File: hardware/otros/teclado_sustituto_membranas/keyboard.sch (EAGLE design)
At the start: 98 parts, among them IC1 74HC32, IC2 74LS244DW

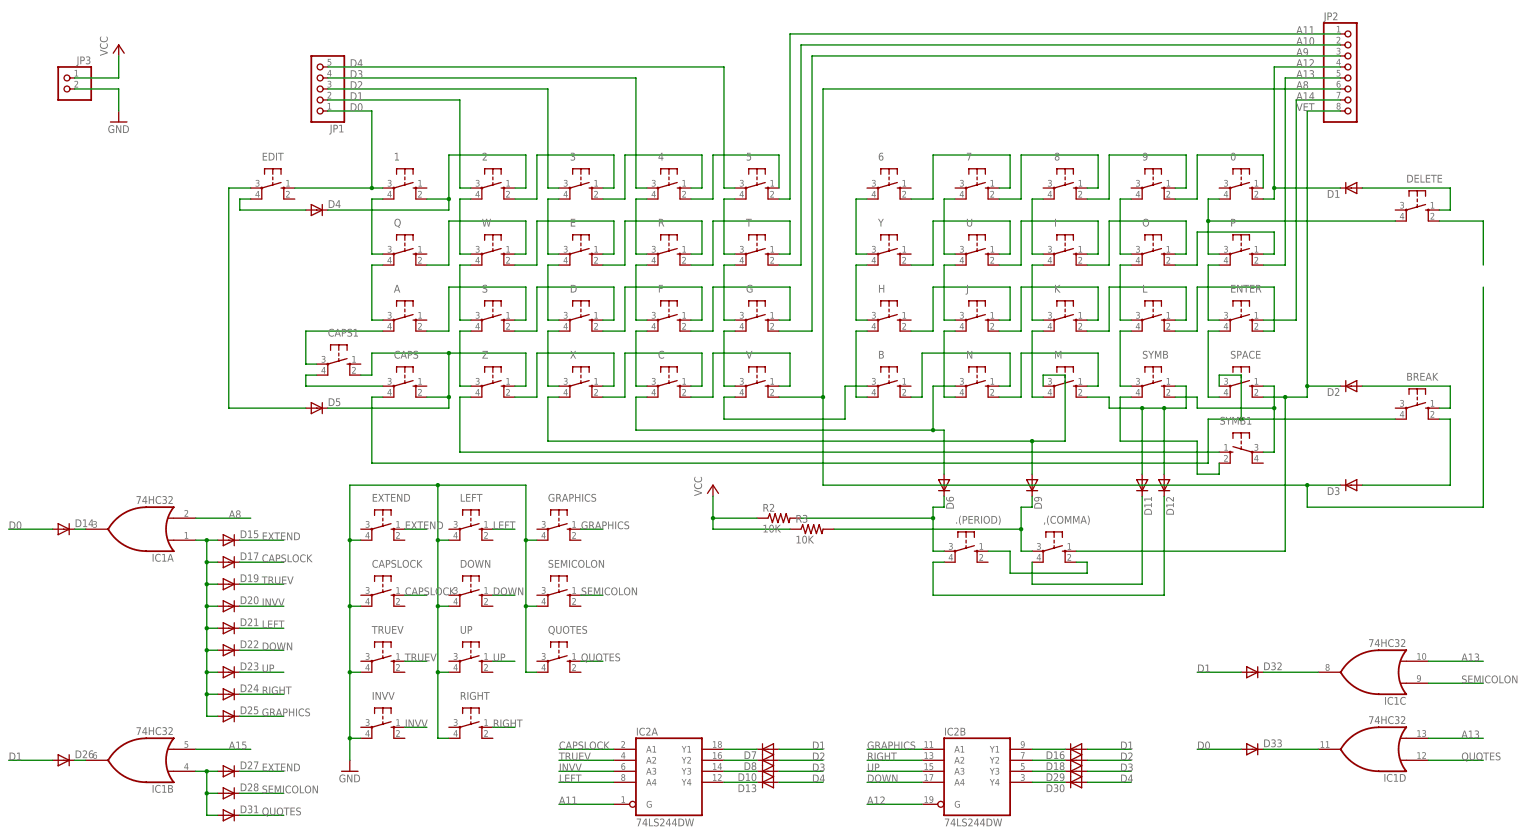
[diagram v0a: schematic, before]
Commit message: 
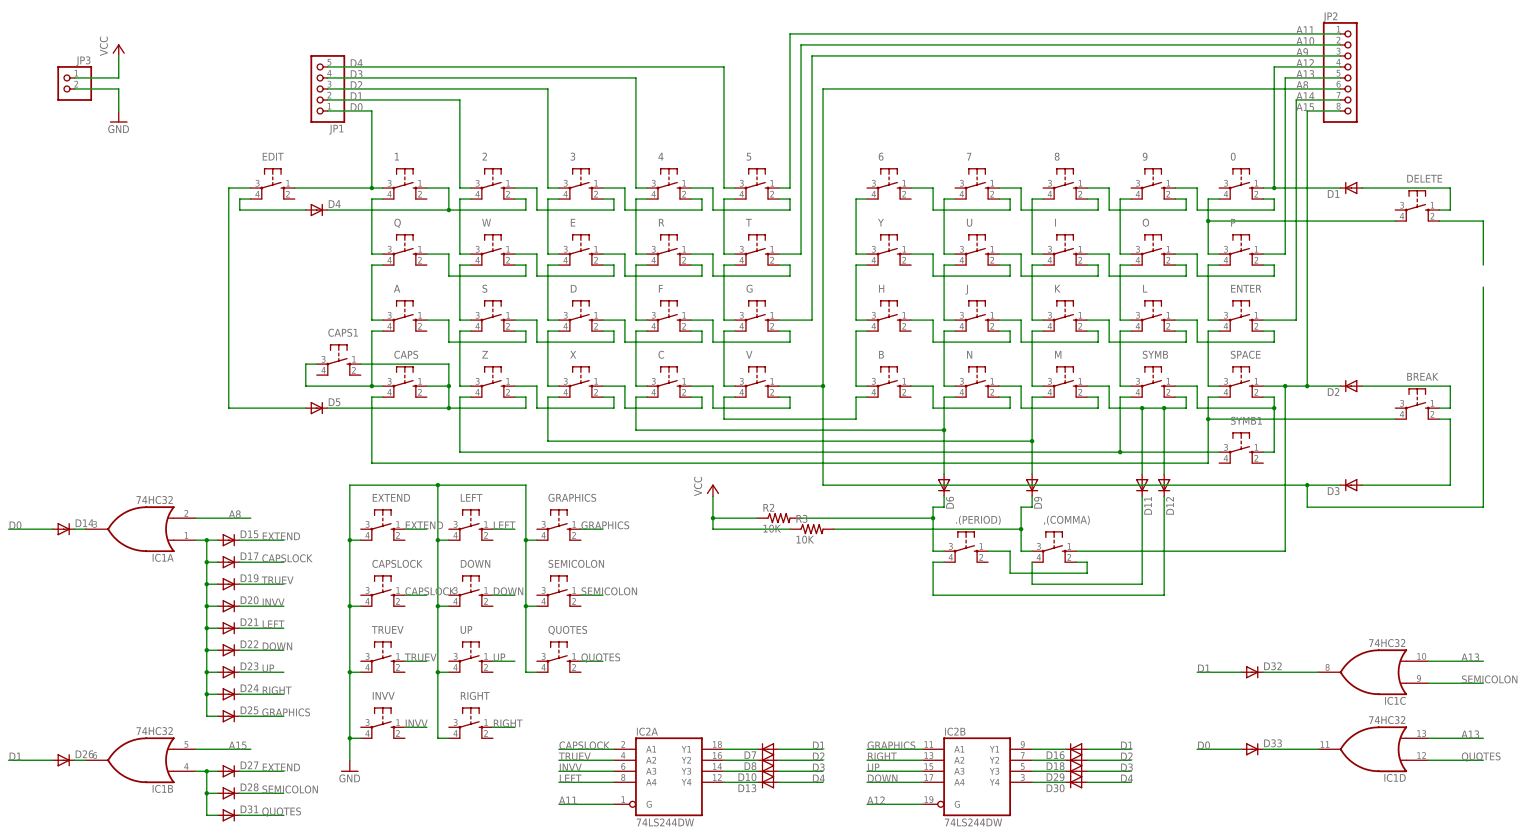
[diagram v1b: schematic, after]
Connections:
- removed net N$91: SYMB.P1, SYMB1.S1
- removed net N$92: F.S1, G.S
- removed net N$93: A.P1, CAPS1.P
- removed net N$94: D.S1, F.S
- removed net N$95: Q.S1, W.S
- removed net VET: ,(COMMA).S, D2.C, JP2.8, SPACE.S1
- new net N$69: SPACE.S1, SYMB.S, SYMB1.S
- new net N$70: D11.A, D12.A, M.S, SYMB.S1
- new net N$72: B.S, N.S1
- net A10: now also T.S; no longer T.S1
- net A11: now also 5.S; no longer 5.S1
- net A12: now also 0.S; no longer 0.S1
- net A13: now also P.S; no longer P.S1
- net A15: now also ,(COMMA).S, D2.C, JP2.8, SPACE.S
- net A8: now also V.S; no longer V.S1
- net A9: now also G.S; no longer G.S1
- net N$10: now also B.P; no longer B.P1
- net N$16: now also SYMB.P1, SYMB1.P; no longer SYMB1.S
- net N$17: now also M.P1; no longer M.P
- net N$18: now also C.P1, D6.A; no longer J.P1
- net N$19: now also B.P1; no longer B.P
- net N$29: now also 3.S, 4.S1; no longer 3.S1, 4.S
- net N$30: now also 4.S, 5.S1; no longer 4.S1, 5.S
- net N$31: now also 2.S, 3.S1; no longer 2.S1, 3.S
- net N$32: now also 1.S, 2.S1; no longer 1.S1, 2.S
- net N$33: now also C.S, V.S1; no longer C.S1, V.S
- net N$34: now also R.S, T.S1; no longer A.S1, S.S
- net N$35: now also E.S; no longer T.S
- net N$36: now also W.S; no longer R.S
- net N$37: now also Q.S; no longer E.S
- net N$38: now also F.S, G.S1; no longer ENTER.S1, L.S1
- net N$39: now also F.S1; no longer S.S1
- net N$40: now also D.S1, S.S; no longer O.S1, P.S
- net N$41: now also A.S, S.S1; no longer I.S1, O.S
- net N$42: now also 0.S1, 9.S; no longer 6.S1, 7.S
- net N$43: now also J.P1; no longer C.P1, D6.A
- net N$46: now also M.P; no longer M.P1
- net N$52: now also SPACE.P; no longer SPACE.P1
- net N$55: now also 8.S; no longer 0.S
- net N$56: now also 7.S; no longer 9.S
- net N$57: now also 6.S; no longer 8.S
- net N$58: now also C.S1, X.S; no longer C.S, X.S1
- net N$59: now also X.S1, Z.S; no longer X.S, Z.S1
- net N$60: now also CAPS.S, CAPS1.S, Z.S1; no longer CAPS.S1, CAPS1.S1, Z.S
- net N$61: now also O.S, P.S1; no longer I.S, U.S1
- net N$62: now also I.S, O.S1; no longer M.S, N.S1
- net N$63: now also I.S1, U.S; no longer K.S1, L.S
- net N$64: now also U.S1, Y.S; no longer U.S, Y.S1
- net N$65: now also ENTER.S1, L.S; no longer J.S1, K.S
- net N$66: now also K.S, L.S1; no longer B.S1, N.S
- net N$67: now also K.S1; no longer H.S1
- net N$68: now also H.S, J.S1; no longer SPACE.S, SYMB.S1, SYMB1.P
- net N$71: now also N.S; no longer D11.A, D12.A, SYMB.S
- net N$8: now also A.P1, CAPS1.P; no longer CAPS1.P1
- net N$9: now also SPACE.P1; no longer SPACE.P

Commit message: Cambio huellas
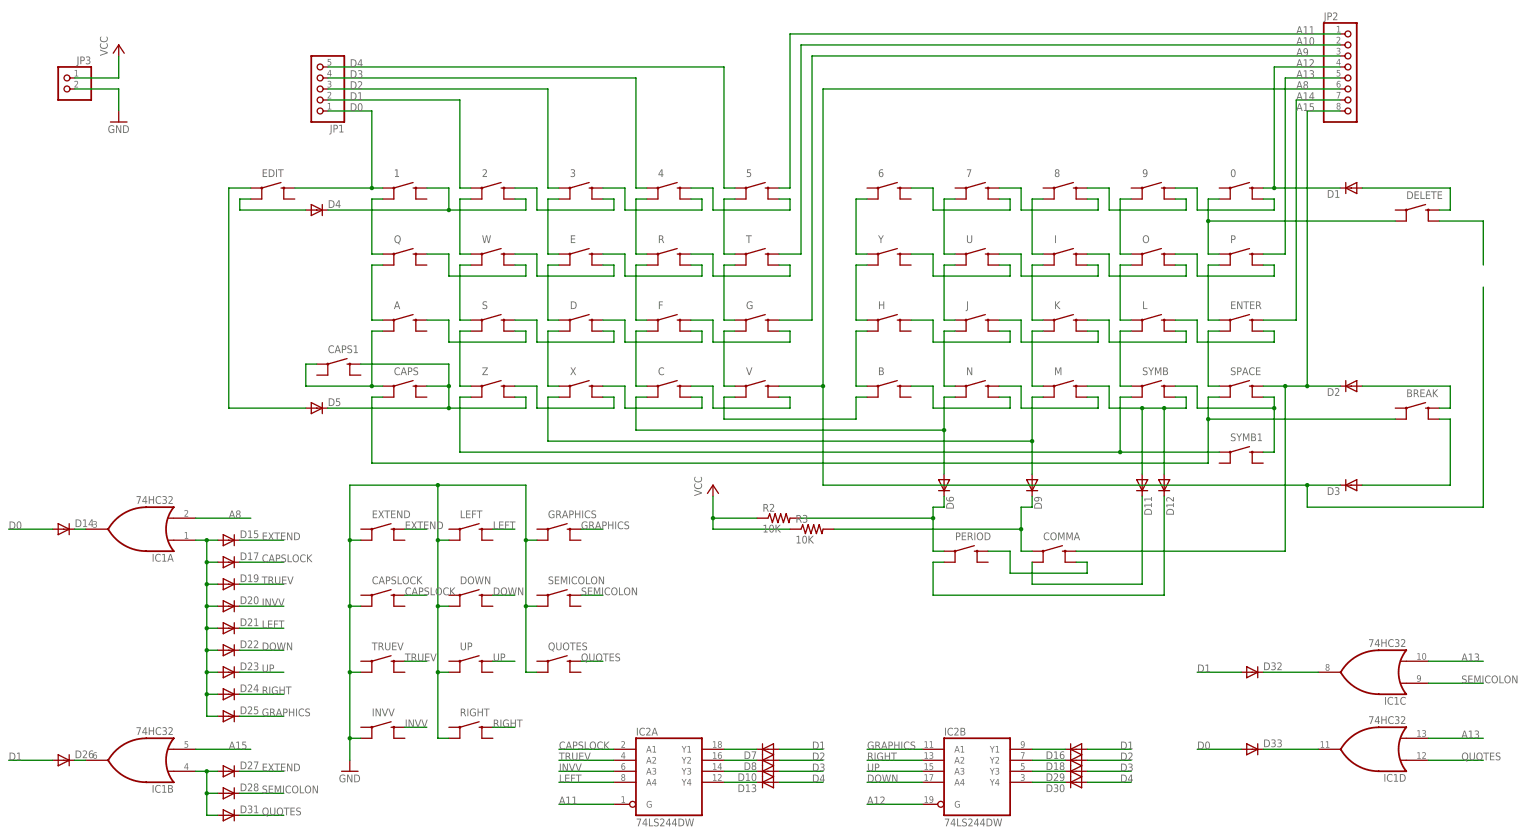
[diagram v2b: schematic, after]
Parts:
- removed ,(COMMA), .(PERIOD): (no value), switch-omron:40-XX
- added COMMA, PERIOD: SWITCH-MOMENTARY-2SMD, SparkFun-Electromechanical:SWITCH-MOMENTARY-2SMD
- 0, 1, 2, 3, 4, 5, 6, 7, 8, 9, A, B, BREAK, C, CAPS, CAPS1, CAPSLOCK, D, DELETE, DOWN, E, EDIT, ENTER, EXTEND, F, G, GRAPHICS, H, I, INVV, J, K, L, LEFT, M, N, O, P, Q, QUOTES, R, RIGHT, S, SEMICOLON, SPACE, SYMB, SYMB1, T, TRUEV, U, UP, V, W, X, Y, Z: value (none) -> SWITCH-MOMENTARY-2SMD; device switch-omron:40-XX -> SparkFun-Electromechanical:SWITCH-MOMENTARY-2SMD
- D1, D10, D11, D12, D13, D14, D15, D16, D17, D18, D19, D2, D20, D21, D22, D23, D24, D25, D26, D27, D28, D29, D3, D30, D31, D32, D33, D4, D5, D6, D7, D8, D9: device diode:DIODE-SMC -> diode:DIODE-SOD323-R
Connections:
- net A10: now also T.2; no longer T.S
- net A11: now also 5.2; no longer 5.S
- net A12: now also 0.2; no longer 0.S
- net A13: now also P.2; no longer P.S
- net A14: now also ENTER.2; no longer ENTER.S
- net A15: now also COMMA.2, SPACE.2; no longer ,(COMMA).S, SPACE.S
- net A8: now also V.2; no longer V.S
- net A9: now also G.2; no longer G.S
- net CAPSLOCK: now also CAPSLOCK.2; no longer CAPSLOCK.S
- net D0: now also 1.1, EDIT.2; no longer 1.P, EDIT.S
- net D1: now also 2.1; no longer 2.P
- net D2: now also 3.1; no longer 3.P
- net D3: now also 4.1; no longer 4.P
- net D4: now also 5.1; no longer 5.P
- net DOWN: now also DOWN.2; no longer DOWN.S
- net EXTEND: now also EXTEND.2; no longer EXTEND.S
- net GND: now also CAPSLOCK.3, DOWN.3, EXTEND.3, GRAPHICS.3, INVV.3, LEFT.3, QUOTES.3, RIGHT.3, SEMICOLON.3, TRUEV.3, UP.3; no longer CAPSLOCK.P1, DOWN.P1, EXTEND.P1, GRAPHICS.P1, INVV.P1, LEFT.P1, QUOTES.P1, RIGHT.P1, SEMICOLON.P1, TRUEV.P1, UP.P1
- net GRAPHICS: now also GRAPHICS.2; no longer GRAPHICS.S
- net INVV: now also INVV.2; no longer INVV.S
- net LEFT: now also LEFT.2; no longer LEFT.S
- net N$1: now also EDIT.3; no longer EDIT.P1
- net N$10: now also B.1, H.3; no longer B.P, H.P1
- net N$11: now also H.1, Y.3; no longer H.P, Y.P1
- net N$12: now also 6.3, Y.1; no longer 6.P1, Y.P
- net N$13: now also 2.3, W.1; no longer 2.P1, W.P
- net N$14: now also S.1, W.3; no longer S.P, W.P1
- net N$15: now also S.3, Z.1; no longer S.P1, Z.P
- net N$16: now also SYMB.3, SYMB1.1, Z.3; no longer SYMB.P1, SYMB1.P, Z.P1
- net N$17: now also M.3, X.3; no longer M.P1, X.P1
- net N$18: now also C.3, N.3; no longer C.P1, N.P1
- net N$19: now also B.3, V.3; no longer B.P1, V.P1
- net N$2: now also EDIT.1; no longer EDIT.P
- net N$20: now also 3.3, E.1; no longer 3.P1, E.P
- net N$21: now also D.1, E.3; no longer D.P, E.P1
- net N$22: now also D.3, X.1; no longer D.P1, X.P
- net N$23: now also 4.3, R.1; no longer 4.P1, R.P
- net N$24: now also F.1, R.3; no longer F.P, R.P1
- net N$25: now also C.1, F.3; no longer C.P, F.P1
- net N$26: now also 5.3, T.1; no longer 5.P1, T.P
- net N$27: now also G.1, T.3; no longer G.P, T.P1
- net N$28: now also G.3, V.1; no longer G.P1, V.P
- net N$29: now also 3.2, 4.4; no longer 3.S, 4.S1
- net N$3: now also BREAK.2; no longer BREAK.S
- net N$30: now also 4.2, 5.4; no longer 4.S, 5.S1
- net N$31: now also 2.2, 3.4; no longer 2.S, 3.S1
- net N$32: now also 1.2, 2.4; no longer 1.S, 2.S1
- net N$33: now also C.2, V.4; no longer C.S, V.S1
- net N$34: now also R.2, T.4; no longer R.S, T.S1
- net N$35: now also E.2, R.4; no longer E.S, R.S1
- net N$36: now also E.4, W.2; no longer E.S1, W.S
- net N$37: now also Q.2, W.4; no longer Q.S, W.S1
- net N$38: now also F.2, G.4; no longer F.S, G.S1
- net N$39: now also D.2, F.4; no longer D.S, F.S1
- net N$4: now also BREAK.4; no longer BREAK.S1
- net N$40: now also D.4, S.2; no longer D.S1, S.S
- net N$41: now also A.2, S.4; no longer A.S, S.S1
- net N$42: now also 0.4, 9.2; no longer 0.S1, 9.S
- net N$43: now also J.3, N.1; no longer J.P1, N.P
- net N$44: now also J.1, U.3; no longer J.P, U.P1
- net N$45: now also 7.3, U.1; no longer 7.P1, U.P
- net N$46: now also K.3, M.1; no longer K.P1, M.P
- net N$47: now also I.3, K.1; no longer I.P1, K.P
- net N$48: now also 8.3, I.1; no longer 8.P1, I.P
- net N$49: now also L.3, SYMB.1; no longer L.P1, SYMB.P
- net N$5: now also DELETE.2; no longer DELETE.S
- net N$50: now also L.1, O.3; no longer L.P, O.P1
- net N$51: now also 9.3, O.1; no longer 9.P1, O.P
- net N$52: now also ENTER.3, SPACE.1; no longer ENTER.P1, SPACE.P
- net N$53: now also ENTER.1, P.3; no longer ENTER.P, P.P1
- net N$54: now also 0.3, DELETE.3, P.1; no longer 0.P1, DELETE.P1, P.P
- net N$55: now also 8.2, 9.4; no longer 8.S, 9.S1
- net N$56: now also 7.2, 8.4; no longer 7.S, 8.S1
- net N$57: now also 6.2, 7.4; no longer 6.S, 7.S1
- net N$58: now also C.4, X.2; no longer C.S1, X.S
- net N$59: now also X.4, Z.2; no longer X.S1, Z.S
- net N$6: now also 1.3, Q.1; no longer 1.P1, Q.P
- net N$60: now also CAPS.2, CAPS1.2, Z.4; no longer CAPS.S, CAPS1.S, Z.S1
- net N$61: now also O.2, P.4; no longer O.S, P.S1
- net N$62: now also I.2, O.4; no longer I.S, O.S1
- net N$63: now also I.4, U.2; no longer I.S1, U.S
- net N$64: now also U.4, Y.2; no longer U.S1, Y.S
- net N$65: now also ENTER.4, L.2; no longer ENTER.S1, L.S
- net N$66: now also K.2, L.4; no longer K.S, L.S1
- net N$67: now also J.2, K.4; no longer J.S, K.S1
- net N$68: now also H.2, J.4; no longer H.S, J.S1
- net N$69: now also SPACE.4, SYMB.2, SYMB1.2; no longer SPACE.S1, SYMB.S, SYMB1.S
- net N$7: now also A.1, Q.3; no longer A.P, Q.P1
- net N$70: now also M.2, SYMB.4; no longer M.S, SYMB.S1
- net N$71: now also M.4, N.2; no longer M.S1, N.S
- net N$72: now also B.2, N.4; no longer B.S, N.S1
- net N$73: now also DELETE.4; no longer DELETE.S1
- net N$76: now also COMMA.4, PERIOD.2; no longer ,(COMMA).S1, .(PERIOD).S
- net N$78: now also COMMA.3; no longer ,(COMMA).P1
- net N$79: now also PERIOD.3; no longer .(PERIOD).P1
- net N$8: now also A.3, CAPS.1, CAPS1.1; no longer A.P1, CAPS.P, CAPS1.P
- net N$82: now also PERIOD.1; no longer .(PERIOD).P
- net N$83: now also COMMA.1; no longer ,(COMMA).P
- net N$9: now also BREAK.3, CAPS.3, SPACE.3; no longer BREAK.P1, CAPS.P1, SPACE.P1
- net QUOTES: now also QUOTES.2; no longer QUOTES.S
- net RIGHT: now also RIGHT.2; no longer RIGHT.S
- net SEMICOLON: now also SEMICOLON.2; no longer SEMICOLON.S
- net TRUEV: now also TRUEV.2; no longer TRUEV.S
- net UP: now also UP.2; no longer UP.S
